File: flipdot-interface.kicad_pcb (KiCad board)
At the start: 4 copper layers, 109.2 x 88.9 mm, 211 parts, among them J1 Conn_02x30_Odd_Even, J2 Conn_02x06_Odd_Even, J3 Screw_Terminal_01x04, J4 Conn_02x06_Odd_Even, Q1 BSS123, Q10 BSS123, Q11 BSS123, Q12 BSS84, Q13 BSS84, Q14 BSS84, Q15 BSS123, Q16 BSS123, Q17 BSS123, Q18 BSS84, Q19 BSS84, Q2 BSS84, Q20 BSS84, Q21 BSS123, Q22 BSS123, Q23 BSS123, Q24 BSS84, Q25 BSS84, Q26 BSS84, Q27 BSS123, Q28 BSS123, Q29 BSS123, Q3 BSS123, Q30 BSS84, Q31 BSS84, Q32 BSS84, Q33 BSS123, Q34 BSS123, Q35 BSS123, Q36 BSS84, Q37 BSS84, Q38 BSS84, Q4 BSS123, Q5 BSS123, Q6 BSS84, Q7 BSS84, Q8 BSS84, Q9 BSS123, U1 74HCT595, U10 74LVC1G19, U11 74HCT595, U12 ULN2803A, U13 74HCT244, U14 LM2734Y, U15 AP1117-33, U2 74HCT595, U3 74HCT595, U4 74HCT595, U5 74HCT595, U6 74HCT595, U7 ULN2803A, U8 ULN2803A, U9 ULN2803A

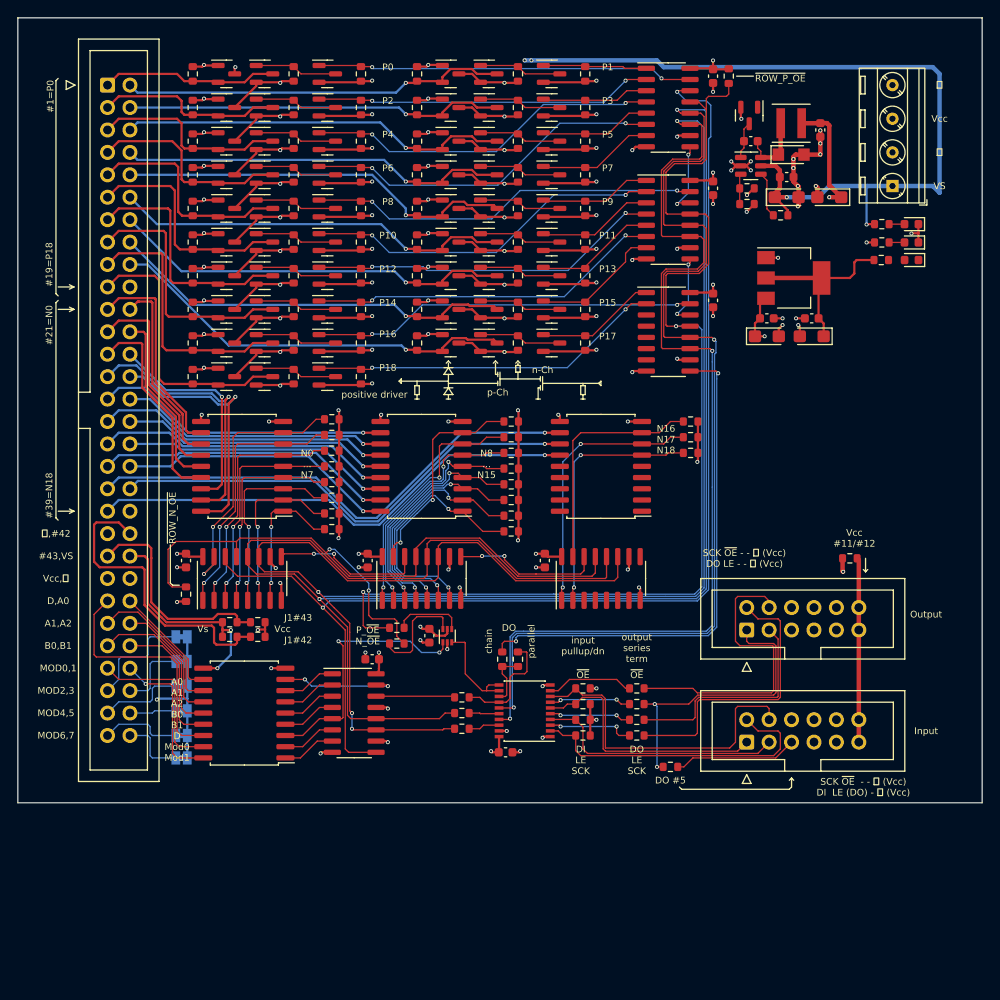
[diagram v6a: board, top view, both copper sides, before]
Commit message: Change positive drivers to a TLE75080-ESD, octal high side driver
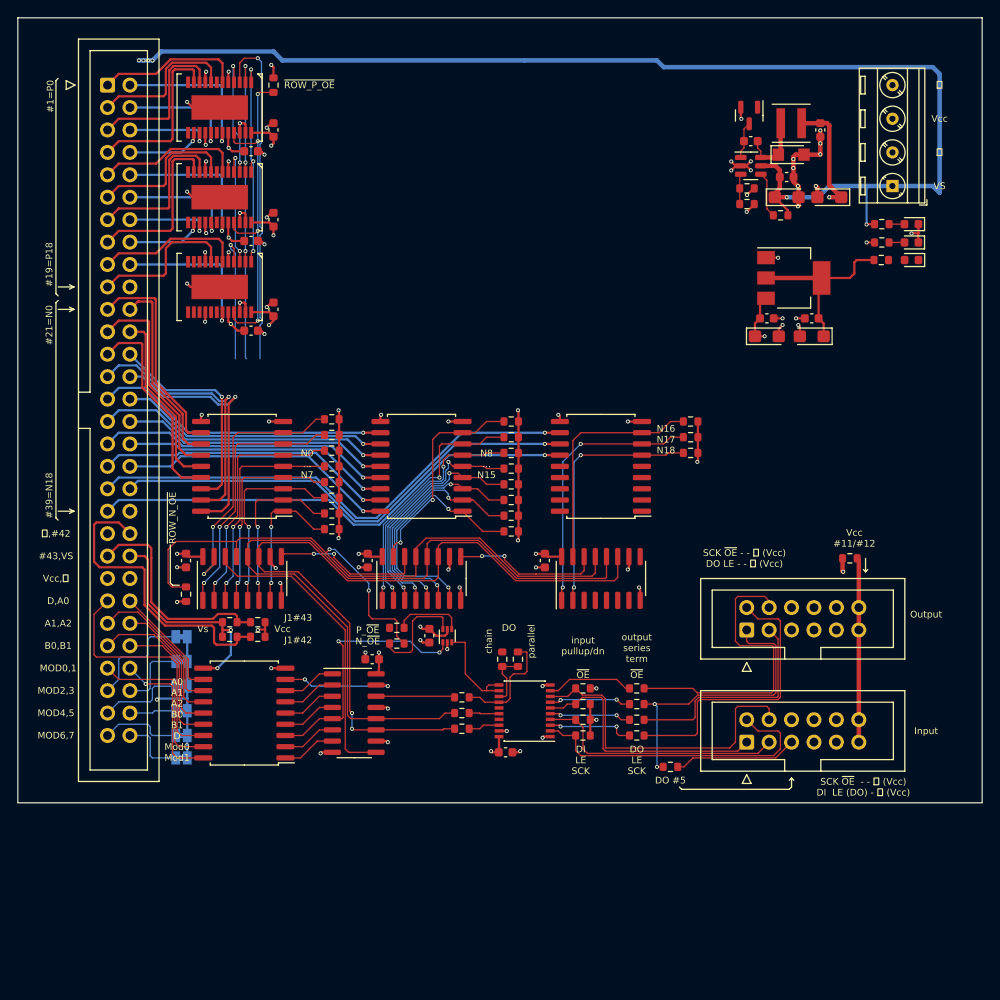
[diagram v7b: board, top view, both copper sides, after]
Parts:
- removed D1, D10, D11, D12, D13, D14, D15, D16, D17, D18, D19, D2, D3, D4, D5, D6, D7, D8, D9: SOT23 A-C-K, Package_TO_SOT_SMD:SOT-23
- removed Q1, Q10, Q11, Q15, Q16, Q17, Q21, Q22, Q23, Q27, Q28, Q29, Q3, Q33, Q34, Q35, Q4, Q5, Q9: BSS123, Package_TO_SOT_SMD:SOT-23
- removed Q12, Q13, Q14, Q18, Q19, Q2, Q20, Q24, Q25, Q26, Q30, Q31, Q32, Q36, Q37, Q38, Q6, Q7, Q8: BSS84, Package_TO_SOT_SMD:SOT-23
- removed R1, R10, R11, R12, R13, R14, R15, R16, R17, R18, R19, R2, R20, R21, R22, R23, R24, R25, R26, R27, R28, R29, R3, R30, R31, R32, R33, R34, R35, R36, R37, R38, R39, R4, R40, R41, R42, R43, R44, R45, R46, R47, R48, R49, R5, R50, R51, R52, R53, R54, R55, R56, R57, R6, R7, R8, R9: 10k, Resistor_SMD:R_0603_1608Metric
- removed U1, U2, U3: 74HCT595, Package_SO:SOIC-16_3.9x9.9mm_P1.27mm
- added C19: 100n, Capacitor_SMD:C_0603_1608Metric, F.Cu at (145.8, 55.9)
- added C20: 100n, Capacitor_SMD:C_0603_1608Metric, F.Cu at (145.8, 66.0)
- added C21: 100n, Capacitor_SMD:C_0603_1608Metric, F.Cu at (145.8, 76.2)
- added U16: tle75080-esd, vogelchr_package_so:Infineon-PG-TSDSO-24-51, F.Cu at (139.7, 53.3)
- added U17: tle75080-esd, vogelchr_package_so:Infineon-PG-TSDSO-24-51, F.Cu at (139.7, 63.5)
- added U18: tle75080-esd, vogelchr_package_so:Infineon-PG-TSDSO-24-51, F.Cu at (139.7, 73.7)
- moved C1 53.0 mm to (143.3, 58.3), turned to 180 degrees
- moved C2 52.7 mm to (143.3, 68.5), turned to 180 degrees
- moved C3 52.4 mm to (143.3, 78.6), turned to 180 degrees
- moved R58 51.6 mm to (145.8, 50.8)
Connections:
- C1 pad 2: VCC -> VS
- C2 pad 2: VCC -> VS
- C3 pad 2: VCC -> VS
- D20 pad 1: (no net) -> unconnected-(D20-Pad1)
- J1 pad 20: (no net) -> unconnected-(J1-Pad20)
- J1 pad 40: (no net) -> unconnected-(J1-Pad40)
- J2 pad 6: (no net) -> unconnected-(J2-Pad6)
- J2 pad 7: (no net) -> unconnected-(J2-Pad7)
- J2 pad 8: (no net) -> unconnected-(J2-Pad8)
- J4 pad 5: (no net) -> unconnected-(J4-Pad5)
- J4 pad 6: (no net) -> unconnected-(J4-Pad6)
- J4 pad 7: (no net) -> unconnected-(J4-Pad7)
- J4 pad 8: (no net) -> unconnected-(J4-Pad8)
- U6 pad 3: (no net) -> unconnected-(U6-Pad3)
- U6 pad 4: (no net) -> unconnected-(U6-Pad4)
- U6 pad 5: (no net) -> unconnected-(U6-Pad5)
- U6 pad 6: (no net) -> unconnected-(U6-Pad6)
- U6 pad 7: (no net) -> unconnected-(U6-Pad7)
- U6 pad 9: (no net) -> /Row Drivers Negative/ROW_N_DO
- U9 pad 1: (no net) -> unconnected-(U9-Pad1)
- U9 pad 14: (no net) -> unconnected-(U9-Pad14)
- U9 pad 15: (no net) -> unconnected-(U9-Pad15)
- U9 pad 16: (no net) -> unconnected-(U9-Pad16)
- U9 pad 17: (no net) -> unconnected-(U9-Pad17)
- U9 pad 18: (no net) -> unconnected-(U9-Pad18)
- U9 pad 2: (no net) -> unconnected-(U9-Pad2)
- U9 pad 3: (no net) -> unconnected-(U9-Pad3)
- U9 pad 4: (no net) -> unconnected-(U9-Pad4)
- U9 pad 5: (no net) -> unconnected-(U9-Pad5)
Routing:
- net /LE: track 303.6 -> 89.8 mm, vias 4 -> 0
- net /SCK: track 301.0 -> 127.1 mm, vias 6 -> 5
- net GND: track 283.0 -> 135.3 mm, vias 89 -> 60
- net /~{ROW_P_OE}: track 124.8 -> 39.0 mm, vias 2 -> 4
- net VS: track 263.7 -> 185.1 mm, vias 29 -> 20
- net /ROW_DI: track 139.3 -> 73.0 mm, vias 2 -> 1
- net /Row Drivers Positive/ROW_G8: track 44.1 -> 0.00 mm, vias 2 -> 0
- net /Row Drivers Positive/ROW_G16: track 43.4 -> 0.00 mm, vias 2 -> 0
- net /DO_P: track 58.4 -> 15.2 mm, vias 2 -> 1
- net /Row Drivers Positive/ROW_G0: track 42.5 -> 0.00 mm, vias 2 -> 0
- net /Row Drivers Positive/ROW_G6: track 40.7 -> 0.00 mm, vias 2 -> 0
- net /Row Drivers Positive/ROW_G10: track 40.6 -> 0.00 mm, vias 2 -> 0
- net /Row Drivers Positive/ROW_G14: track 40.1 -> 0.00 mm, vias 2 -> 0
- net /Row Drivers Positive/ROW_G4: track 40.1 -> 0.00 mm, vias 2 -> 0
- net /Row Drivers Positive/ROW_G18: track 40.0 -> 0.00 mm, vias 2 -> 0
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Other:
- board text removed: "P0"
- board text removed: "P1"
- board text removed: "P10"
- board text removed: "P11"
- board text removed: "P12"
- board text removed: "P13"
- board text removed: "P14"
- board text removed: "P15"
- board text removed: "P16"
- board text removed: "P17"
- board text removed: "P18"
- board text removed: "P2"
- board text removed: "P3"
- board text removed: "P4"
- board text removed: "P5"
- board text removed: "P6"
- board text removed: "P7"
- board text removed: "P8"
- board text removed: "P9"
- board text removed: "n-Ch"
- board text removed: "p-Ch"
- board text removed: "positive driver"
